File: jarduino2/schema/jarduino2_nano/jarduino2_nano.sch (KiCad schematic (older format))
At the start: 34 parts, among them J1 Power, J2 Interface, J3 Pompe 1, J4 Pompe 2, Q1 Q_NPN_BCE, Q2 Q_NPN_BCE, U1 RFB-0505S, U2 RtcArduino

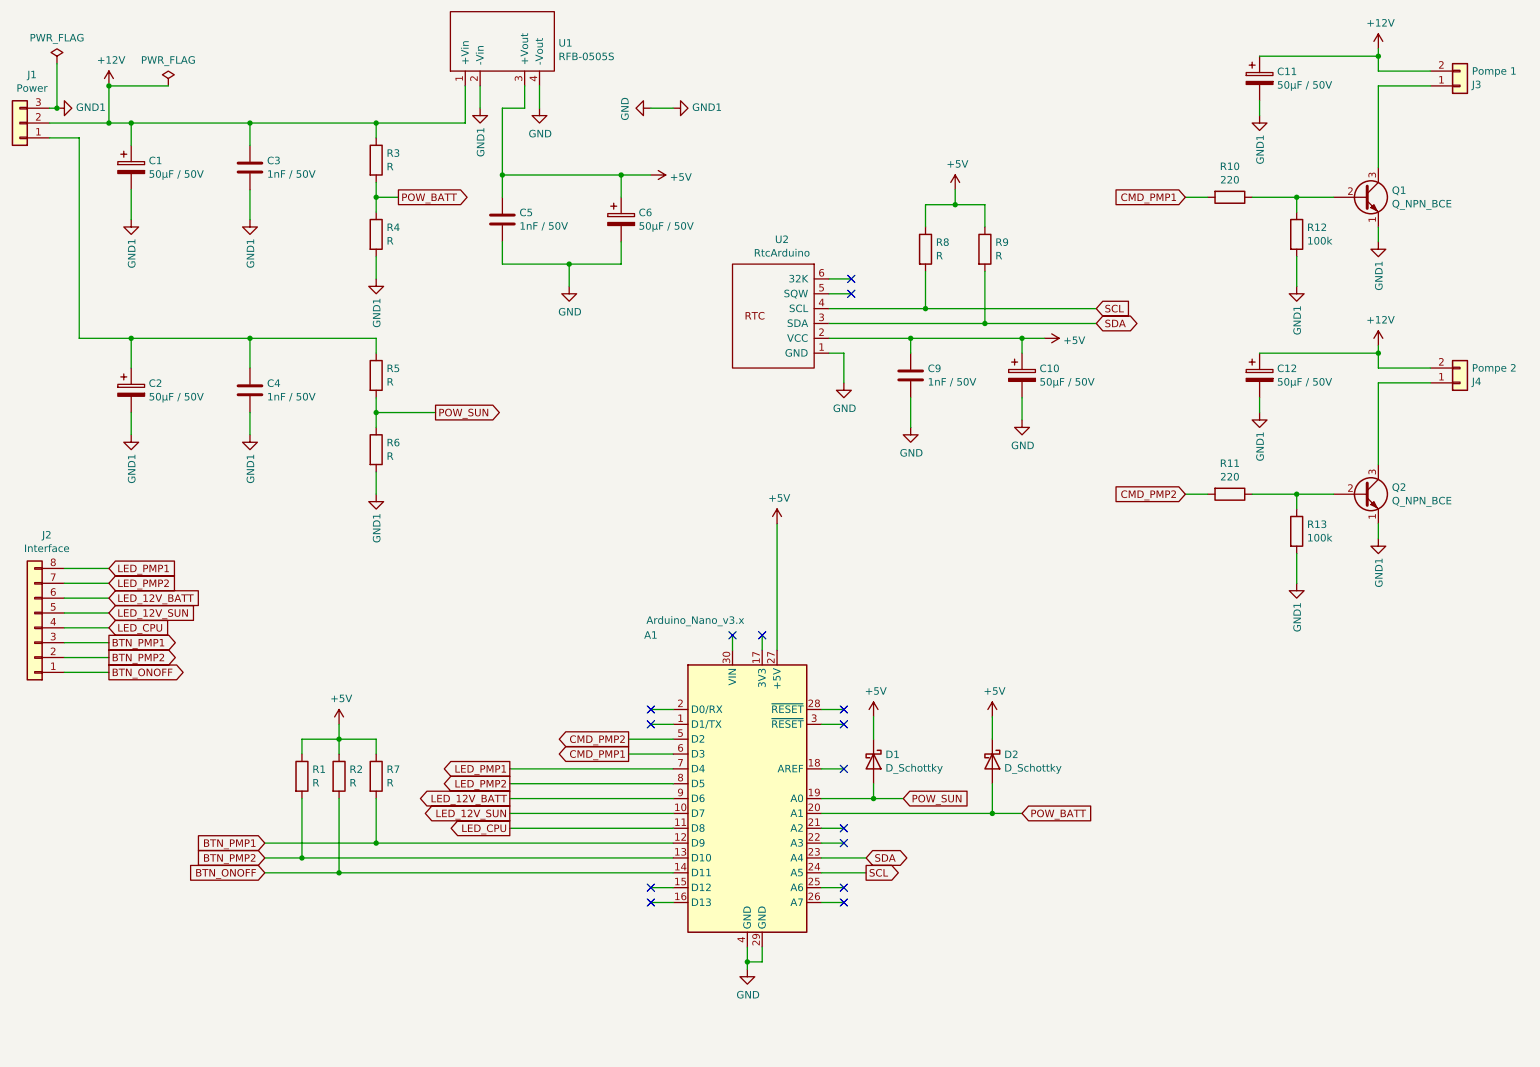
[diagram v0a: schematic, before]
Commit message: Ajout capteur de temp et hum + ext serie
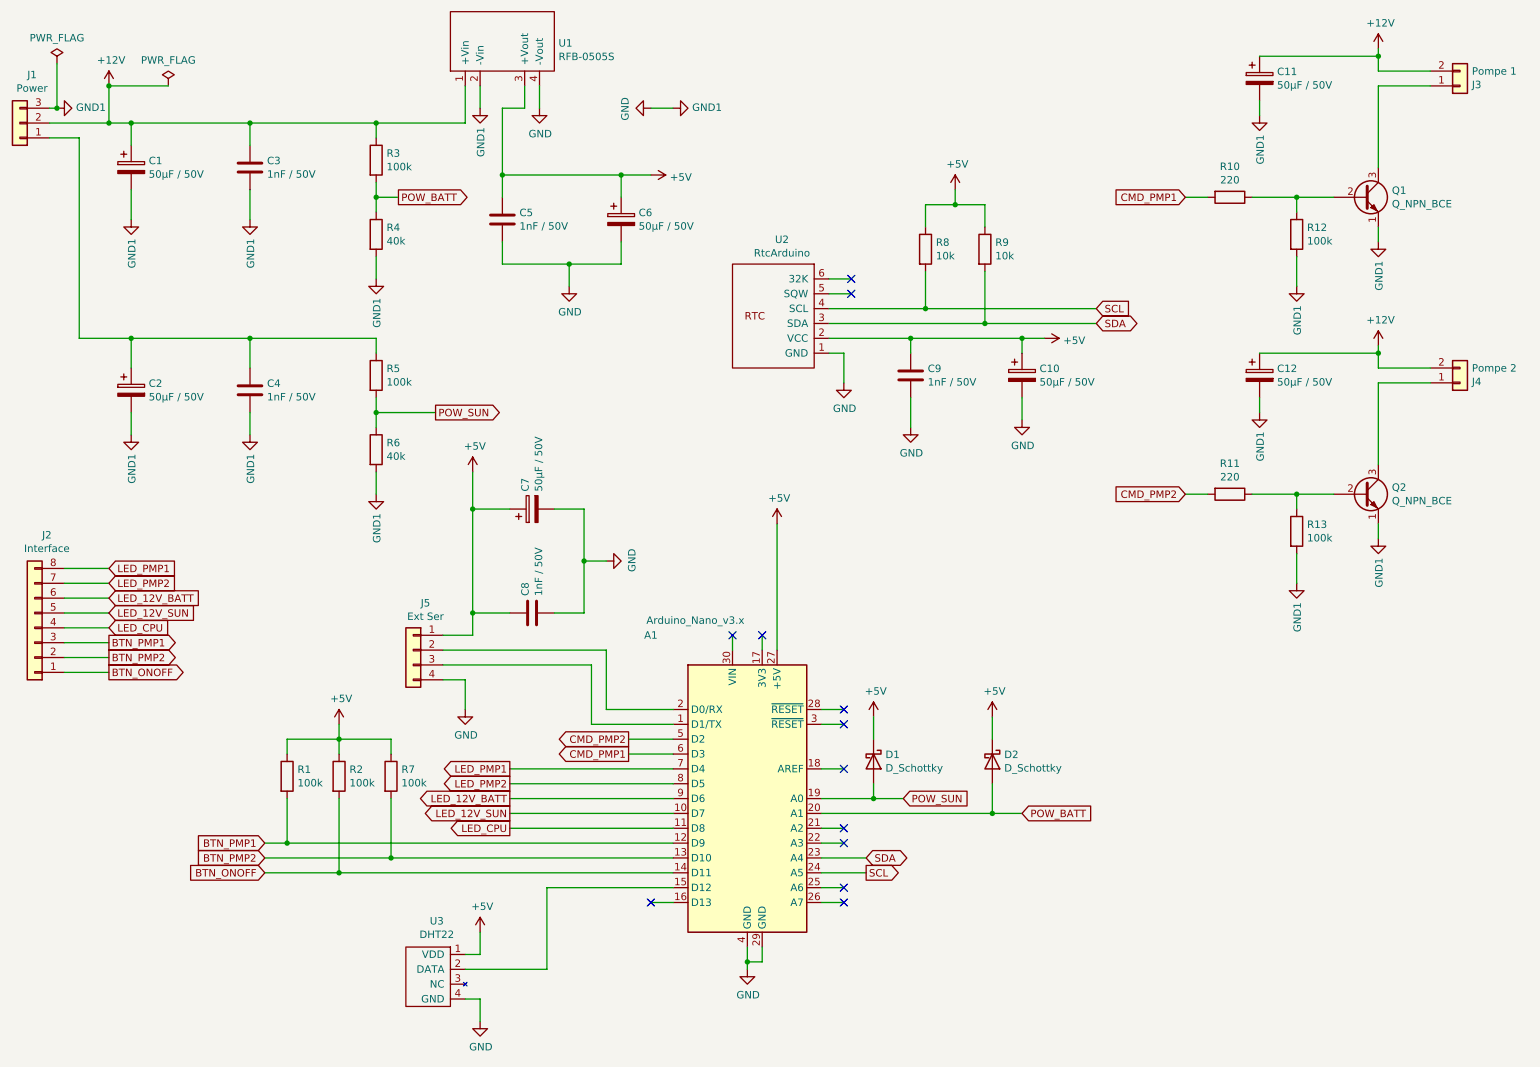
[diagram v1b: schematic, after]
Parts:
- added C7: 50µF / 50V, Capacitor_THT:CP_Radial_D10.0mm_P7.50mm, symbol Device:CP
- added C8: 1nF / 50V, Capacitor_THT:C_Rect_L10.0mm_W4.0mm_P7.50mm_MKS4, symbol Device:C
- added J5: Ext Ser, Connector_PinHeader_2.54mm:PinHeader_1x04_P2.54mm_Vertical, symbol Connector_Generic:Conn_01x04
- added U3: DHT22, bpc:BPC_DHT22, symbol bpc:DHT22
- R1, R2, R3, R5, R7: value R -> 100k
- R4, R6: value R -> 40k
- R8, R9: value R -> 10k
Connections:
- net +5V: now also C7.1, C8.1, J5.1 (Pin_1), U3.1 (VDD)
- net BTN_PMP1: now also R1.2; no longer R7.2
- net BTN_PMP2: now also R7.2; no longer R1.2
- net GND: now also C7.2, C8.2, J5.4 (Pin_4), U3.4 (GND)
- net at A1.1 (D1/TX): now also J5.3 (Pin_3)
- net at A1.15 (D12): now also U3.2 (DATA)
- net at A1.2 (D0/RX): now also J5.2 (Pin_2)
- no-connect marks 15 -> 12
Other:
- moved on the sheet: R1, R7
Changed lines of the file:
@@
 encoding utf-8
 Sheet 1 1
-Title ""
-Date ""
-Rev ""
-Comp ""
+Title "Jarduino 2 - Carte Power Nano Autonome"
+Date "2022-03-19"
+Rev "A"
+Comp "BPC"
 Comment1 ""
 Comment2 ""
@@
 P 3350 1600
 F 0 "R3" H 3420 1646 50  0000 L CNN
-F 1 "R" H 3420 1555 50  0000 L CNN
+F 1 "100k" H 3420 1555 50  0000 L CNN
 F 2 "Resistor_THT:R_Axial_DIN0411_L9.9mm_D3.6mm_P5.08mm_Vertical" V 3280 1600 50  0001 C CNN
 F 3 "~" H 3350 1600 50  0001 C CNN
@@
 P 3350 2100
 F 0 "R4" H 3420 2146 50  0000 L CNN
-F 1 "R" H 3420 2055 50  0000 L CNN
+F 1 "40k" H 3420 2055 50  0000 L CNN
 F 2 "Resistor_THT:R_Axial_DIN0411_L9.9mm_D3.6mm_P5.08mm_Vertical" V 3280 2100 50  0001 C CNN
 F 3 "~" H 3350 2100 50  0001 C CNN
@@
 P 3350 3050
 F 0 "R5" H 3420 3096 50  0000 L CNN
-F 1 "R" H 3420 3005 50  0000 L CNN
+F 1 "100k" H 3420 3005 50  0000 L CNN
 F 2 "Resistor_THT:R_Axial_DIN0411_L9.9mm_D3.6mm_P5.08mm_Vertical" V 3280 3050 50  0001 C CNN
 F 3 "~" H 3350 3050 50  0001 C CNN
@@
 P 3350 3550
 F 0 "R6" H 3420 3596 50  0000 L CNN
-F 1 "R" H 3420 3505 50  0000 L CNN
+F 1 "40k" H 3420 3505 50  0000 L CNN
 F 2 "Resistor_THT:R_Axial_DIN0411_L9.9mm_D3.6mm_P5.08mm_Vertical" V 3280 3550 50  0001 C CNN
 F 3 "~" H 3350 3550 50  0001 C CNN
@@
 P 7050 2200
 F 0 "R8" H 7120 2246 50  0000 L CNN
-F 1 "R" H 7120 2155 50  0000 L CNN
+F 1 "10k" H 7120 2155 50  0000 L CNN
 F 2 "Resistor_THT:R_Axial_DIN0411_L9.9mm_D3.6mm_P5.08mm_Vertical" V 6980 2200 50  0001 C CNN
 F 3 "~" H 7050 2200 50  0001 C CNN
@@
 P 7450 2200
 F 0 "R9" H 7520 2246 50  0000 L CNN
-F 1 "R" H 7520 2155 50  0000 L CNN
+F 1 "10k" H 7520 2155 50  0000 L CNN
 F 2 "Resistor_THT:R_Axial_DIN0411_L9.9mm_D3.6mm_P5.08mm_Vertical" V 7380 2200 50  0001 C CNN
 F 3 "~" H 7450 2200 50  0001 C CNN
@@
 L Device:R R7
 U 1 1 60BA1689
-P 3350 5750
-F 0 "R7" H 3420 5796 50  0000 L CNN
-F 1 "R" H 3420 5705 50  0000 L CNN
-F 2 "Resistor_THT:R_Axial_DIN0411_L9.9mm_D3.6mm_P5.08mm_Vertical" V 3280 5750 50  0001 C CNN
-F 3 "~" H 3350 5750 50  0001 C CNN
-	1    3350 5750
+P 3450 5750
+F 0 "R7" H 3520 5796 50  0000 L CNN
+F 1 "100k" H 3520 5705 50  0000 L CNN
+F 2 "Resistor_THT:R_Axial_DIN0411_L9.9mm_D3.6mm_P5.08mm_Vertical" V 3380 5750 50  0001 C CNN
+F 3 "~" H 3450 5750 50  0001 C CNN
+	1    3450 5750
 	1    0    0    -1
 $EndComp
@@
 L Device:R R1
 U 1 1 60BA1FFA
-P 2850 5750
-F 0 "R1" H 2920 5796 50  0000 L CNN
-F 1 "R" H 2920 5705 50  0000 L CNN
-F 2 "Resistor_THT:R_Axial_DIN0411_L9.9mm_D3.6mm_P5.08mm_Vertical" V 2780 5750 50  0001 C CNN
-F 3 "~" H 2850 5750 50  0001 C CNN
-	1    2850 5750
+P 2750 5750
+F 0 "R1" H 2820 5796 50  0000 L CNN
+F 1 "100k" H 2820 5705 50  0000 L CNN
+F 2 "Resistor_THT:R_Axial_DIN0411_L9.9mm_D3.6mm_P5.08mm_Vertical" V 2680 5750 50  0001 C CNN
+F 3 "~" H 2750 5750 50  0001 C CNN
+	1    2750 5750
 	1    0    0    -1
 $EndComp
@@
 Wire Wire Line
 	3100 5400 3100 5500
-Wire Wire Line
-	3100 5500 3350 5500
-Wire Wire Line
-	3350 5500 3350 5600
-Wire Wire Line
-	3100 5500 2850 5500
-Wire Wire Line
-	2850 5500 2850 5600
 Connection ~ 3100 5500
-Wire Wire Line
-	3350 6200 3350 5900
-Wire Wire Line
-	2850 6300 2850 5900
 Text GLabel 2600 6200 0    50   Input ~ 0
 BTN_PMP1
 Text GLabel 2600 6300 0    50   Input ~ 0
 BTN_PMP2
-Wire Wire Line
-	2600 6200 3350 6200
-Wire Wire Line
-	2850 6300 2600 6300
-Wire Wire Line
-	5350 6200 3350 6200
-Connection ~ 3350 6200
-Wire Wire Line
-	2850 6300 5350 6300
-Connection ~ 2850 6300
 $Comp
 L Device:R R2
@@
 P 3100 5750
 F 0 "R2" H 3170 5796 50  0000 L CNN
-F 1 "R" H 3170 5705 50  0000 L CNN
+F 1 "100k" H 3170 5705 50  0000 L CNN
 F 2 "Resistor_THT:R_Axial_DIN0411_L9.9mm_D3.6mm_P5.08mm_Vertical" V 3030 5750 50  0001 C CNN
 F 3 "~" H 3100 5750 50  0001 C CNN
@@
 Wire Wire Line
 	1250 5050 1550 5050
-NoConn ~ 5200 5300
-NoConn ~ 5200 5400
-NoConn ~ 5200 6500
 NoConn ~ 5200 6600
 NoConn ~ 6500 6600
@@
 	5750 4800 5750 4900
 Wire Wire Line
-	5350 5300 5200 5300
-Wire Wire Line
-	5200 5400 5350 5400
-Wire Wire Line
-	5200 6500 5350 6500
-Wire Wire Line
 	5350 6600 5200 6600
 Wire Wire Line
@@
 Wire Wire Line
 	5200 1250 5350 1250
+$Comp
+L bpc:DHT22 U3
+U 1 1 6236E527
+P 3850 6950
+F 0 "U3" H 3942 7175 50  0000 C CNN
+F 1 "DHT22" H 3942 7084 50  0000 C CNN
+F 2 "bpc:BPC_DHT22" H 3850 7050 50  0001 C CNN
+F 3 "" H 3850 7050 50  0001 C CNN
+	1    3850 6950
+	-1   0    0    -1
+$EndComp
+$Comp
+L power:GND #PWR04
+U 1 1 623708C4
+P 4050 7400
+F 0 "#PWR04" H 4050 7150 50  0001 C CNN
+F 1 "GND" H 4055 7227 50  0000 C CNN
+F 2 "" H 4050 7400 50  0001 C CNN
+F 3 "" H 4050 7400 50  0001 C CNN
+	1    4050 7400
+	1    0    0    -1
+$EndComp
+Wire Wire Line
+	4050 7400 4050 7250
+Wire Wire Line
+	4050 7250 3950 7250
+$Comp
+L power:+5V #PWR03
+U 1 1 6237800B
+P 4050 6800
+F 0 "#PWR03" H 4050 6650 50  0001 C CNN
+F 1 "+5V" H 4065 6973 50  0000 C CNN
+F 2 "" H 4050 6800 50  0001 C CNN
+F 3 "" H 4050 6800 50  0001 C CNN
+	1    4050 6800
+	1    0    0    -1
+$EndComp
+Wire Wire Line
+	4050 6800 4050 6950
+Wire Wire Line
+	4050 6950 3950 6950
+Wire Wire Line
+	3950 7050 4500 7050
+Wire Wire Line
+	4500 7050 4500 6500
+Wire Wire Line
+	4500 6500 5350 6500
+$Comp
+L Connector_Generic:Conn_01x04 J5
+U 1 1 62387C20
+P 3600 4900
+F 0 "J5" H 3518 5217 50  0000 C CNN
+F 1 "Ext Ser" H 3518 5126 50  0000 C CNN
+F 2 "Connector_PinHeader_2.54mm:PinHeader_1x04_P2.54mm_Vertical" H 3600 4900 50  0001 C CNN
+F 3 "~" H 3600 4900 50  0001 C CNN
+	1    3600 4900
+	-1   0    0    -1
+$EndComp
+$Comp
+L power:GND #PWR01
+U 1 1 6238AD28
+P 3950 5300
+F 0 "#PWR01" H 3950 5050 50  0001 C CNN
+F 1 "GND" H 3955 5127 50  0000 C CNN
+F 2 "" H 3950 5300 50  0001 C CNN
+F 3 "" H 3950 5300 50  0001 C CNN
+	1    3950 5300
+	1    0    0    -1
+$EndComp
+Wire Wire Line
+	4900 4900 4900 5300
+Wire Wire Line
+	4800 5000 4800 5400
+Wire Wire Line
+	4900 5300 5350 5300
+Wire Wire Line
+	4800 5400 5350 5400
+$Comp
+L Device:CP C7
+U 1 1 623B2963
+P 4400 3950
+F 0 "C7" H 4518 3996 50  0000 L CNN
+F 1 "50µF / 50V" H 4518 3905 50  0000 L CNN
+F 2 "Capacitor_THT:CP_Radial_D10.0mm_P7.50mm" H 4438 3800 50  0001 C CNN
+F 3 "~" H 4400 3950 50  0001 C CNN
+	1    4400 3950
+	0    -1   -1   0
+$EndComp
+Wire Wire Line
+	3800 4900 4900 4900
+Wire Wire Line
+	3800 5000 4800 5000
+Wire Wire Line
+	3950 5300 3950 5100
+Wire Wire Line
+	3950 5100 3800 5100
+Wire Wire Line
+	3800 4800 4000 4800
+Wire Wire Line
+	4000 4800 4000 4650
+$Comp
+L Device:C C8
+U 1 1 623EECA4
+P 4400 4650
+F 0 "C8" H 4515 4696 50  0000 L CNN
+F 1 "1nF / 50V" H 4515 4605 50  0000 L CNN
+F 2 "Capacitor_THT:C_Rect_L10.0mm_W4.0mm_P7.50mm_MKS4" H 4438 4500 50  0001 C CNN
+F 3 "~" H 4400 4650 50  0001 C CNN
+	1    4400 4650
+	0    -1   -1   0
+$EndComp
+Connection ~ 4000 4650
+Wire Wire Line
+	4000 4650 4250 4650
+$Comp
+L power:GND #PWR05
+U 1 1 6240A71D
+P 4900 4300
+F 0 "#PWR05" H 4900 4050 50  0001 C CNN
+F 1 "GND" H 4905 4127 50  0000 C CNN
+F 2 "" H 4900 4300 50  0001 C CNN
+F 3 "" H 4900 4300 50  0001 C CNN
+	1    4900 4300
+	0    -1   -1   0
+$EndComp
+$Comp
+L power:+5V #PWR02
+U 1 1 6240B027
+P 4000 3700
+F 0 "#PWR02" H 4000 3550 50  0001 C CNN
+F 1 "+5V" H 4015 3873 50  0000 C CNN
+F 2 "" H 4000 3700 50  0001 C CNN
+F 3 "" H 4000 3700 50  0001 C CNN
+	1    4000 3700
+	1    0    0    -1
+$EndComp
+Wire Wire Line
+	4000 3700 4000 3950
+Wire Wire Line
+	4000 3950 4000 4650
+Connection ~ 4000 3950
+Wire Wire Line
+	4750 3950 4750 4300
+Wire Wire Line
+	4750 4300 4900 4300
+Connection ~ 4750 4300
+Wire Wire Line
+	4750 4300 4750 4650
+Wire Wire Line
+	4550 4650 4750 4650
+Wire Wire Line
+	2600 6300 3450 6300
+Wire Wire Line
+	2600 6200 2750 6200
+Wire Wire Line
+	3450 5500 3450 5600
+Wire Wire Line
+	3100 5500 3450 5500
+Wire Wire Line
+	3450 5900 3450 6300
+Connection ~ 3450 6300
+Wire Wire Line
+	3450 6300 5350 6300
+Wire Wire Line
+	2750 5500 2750 5600
+Wire Wire Line
+	2750 5500 3100 5500
+Wire Wire Line
+	2750 5900 2750 6200
+Connection ~ 2750 6200
+Wire Wire Line
+	2750 6200 5350 6200
+Wire Wire Line
+	4550 3950 4750 3950
+Wire Wire Line
+	4000 3950 4250 3950
 $EndSCHEMATC

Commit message: Amélioration 3d / libs
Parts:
- A1: footprint Module:Arduino_Nano -> bpc:BPC_Arduino_Nano
- U3: symbol bpc:DHT22 -> bpc:BPC_DHT22
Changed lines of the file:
@@
 F 0 "A1" H 5200 7000 50  0000 C CNN
 F 1 "Arduino_Nano_v3.x" H 5500 7100 50  0000 C CNN
-F 2 "Module:Arduino_Nano" H 5850 5900 50  0001 C CIN
+F 2 "bpc:BPC_Arduino_Nano" H 5850 5900 50  0001 C CIN
 F 3 "http://www.mouser.com/pdfdocs/Gravitech_Arduino_Nano3_0.pdf" H 5850 5900 50  0001 C CNN
 	1    5850 5900
@@
 	5200 1250 5350 1250
 $Comp
-L bpc:DHT22 U3
+L bpc:BPC_DHT22 U3
 U 1 1 6236E527
 P 3850 6950
